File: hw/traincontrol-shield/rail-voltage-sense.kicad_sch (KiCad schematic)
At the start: 2 parts

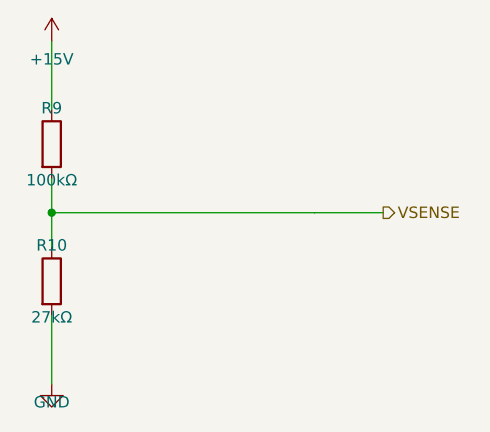
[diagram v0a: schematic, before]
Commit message: Schematic updates by hand.
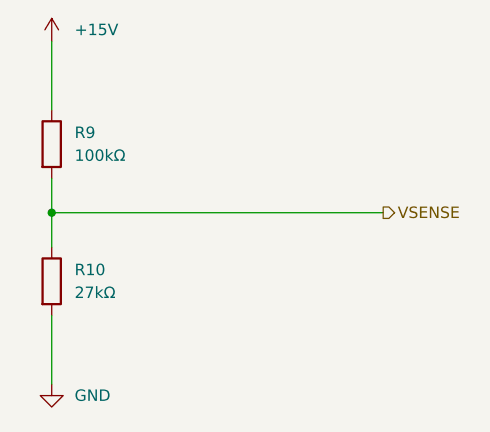
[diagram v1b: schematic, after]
